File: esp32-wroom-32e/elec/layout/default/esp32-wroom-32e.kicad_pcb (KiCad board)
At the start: 2 copper layers, 225.7 x 100.8 mm, 0 parts

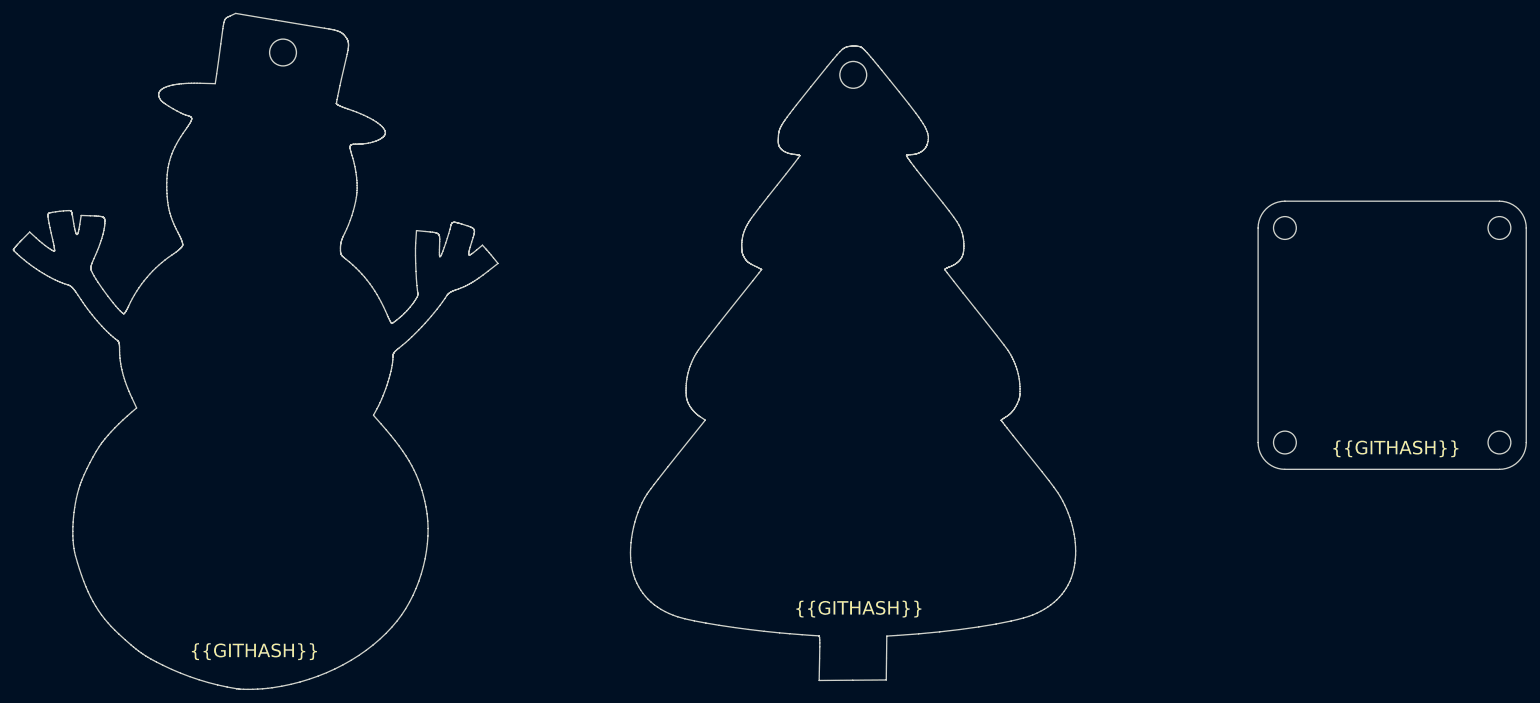
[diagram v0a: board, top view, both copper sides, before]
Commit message: added screw terminals for esp32 pcb
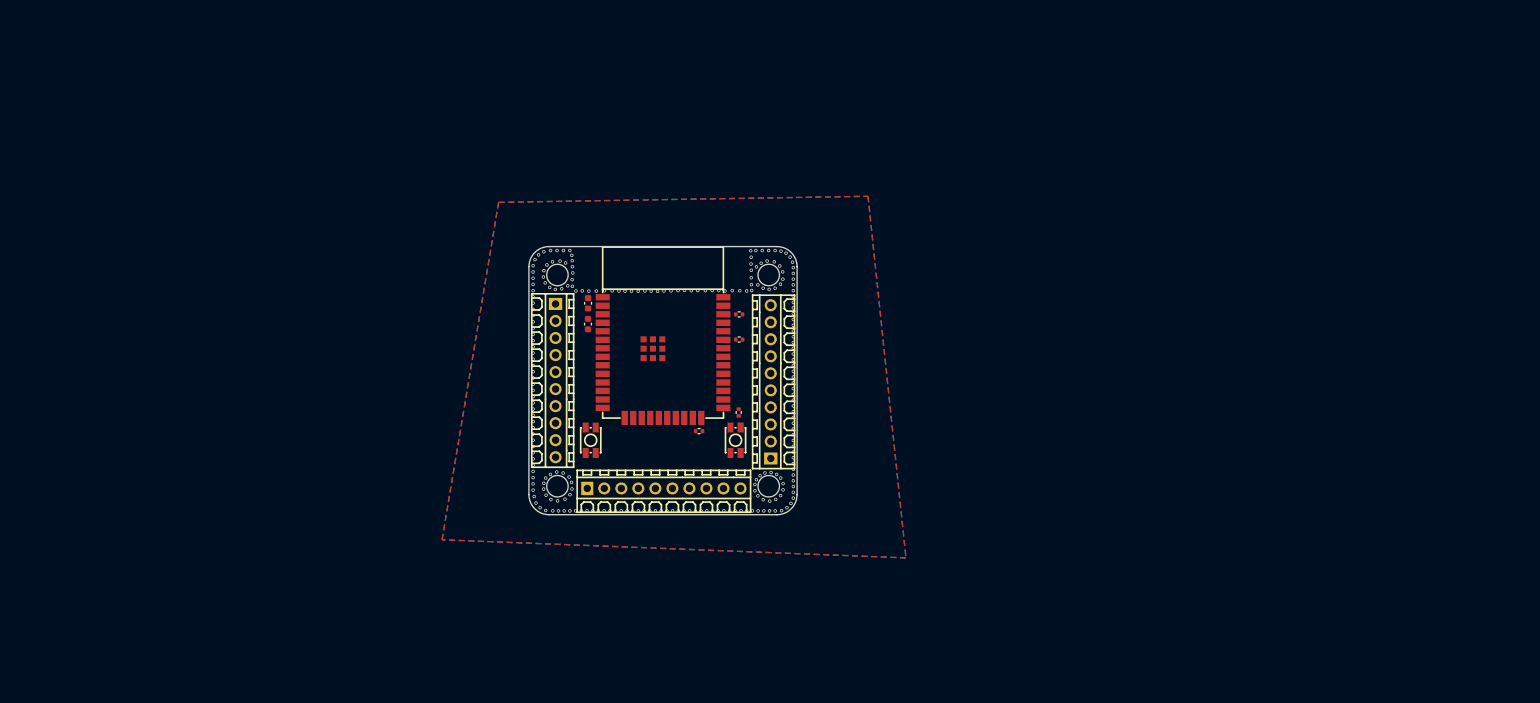
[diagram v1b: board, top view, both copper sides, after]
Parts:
- added C1: 10V 10uF X5R ±10% 0603 Multilayer Ceramic Capacitors MLCC -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, lib:C0603, F.Cu at (121.7, 93.0)
- added C2: 50V 1uF X5R ±10% 0603 Multilayer Ceramic Capacitors MLCC - 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, lib:C0603, F.Cu at (121.7, 96.1)
- added R1: 62.5mW Thick Film Resistors 50V ±100ppm/℃ ±1% 2kΩ 0402 Chip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, lib:R0402, F.Cu at (144.2, 98.4)
- added R2: 62.5mW Thick Film Resistors 50V ±100ppm/℃ ±1% 2kΩ 0402 Chip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, lib:R0402, F.Cu at (144.2, 94.7)
- added R3: 62.5mW Thick Film Resistors 50V ±100ppm/℃ ±1% 5.1kΩ 0402 Ch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, lib:R0402, F.Cu at (138.2, 112.1)
- added R4: 62.5mW Thick Film Resistors 50V ±100ppm/℃ ±1% 100kΩ 0402 Ch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, lib:R0402, F.Cu at (144.1, 109.3)
- added U1: , lib:WIFI-SMD_ESP32-WROOM-32E, F.Cu at (132.8, 101.1)
- added U10: , lib:MountingHole_3.2mm_M3, F.Cu at (117.1, 120.3)
- added U2: , lib:SW-SMD_4P-L3.7-W3.0-P1.50-LS4.7, F.Cu at (143.7, 113.5)
- added U3: , lib:SW-SMD_4P-L3.7-W3.0-P1.50-LS4.7, F.Cu at (122.1, 113.5)
- added U4: , lib:CONN-TH_10P-P2.54_MX128-2.54-10P-GN01-CU-Y-A, F.Cu at (116.8, 104.5)
- added U5: , lib:CONN-TH_10P-P2.54_MX128-2.54-10P-GN01-CU-Y-A, F.Cu at (133.0, 120.6)
- added U6: , lib:CONN-TH_10P-P2.54_MX128-2.54-10P-GN01-CU-Y-A, F.Cu at (148.9, 104.7)
- added U7: , lib:MountingHole_3.2mm_M3, F.Cu at (148.6, 88.8)
- added U8: , lib:MountingHole_3.2mm_M3, F.Cu at (148.6, 120.3)
- added U9: , lib:MountingHole_3.2mm_M3, F.Cu at (117.1, 88.8)
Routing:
- net gnd: vias 0 -> 231
- added copper zone on B.Cu, net gnd
- added copper zone on F.Cu, net gnd
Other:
- board size 225.7 x 100.8 mm -> 40 x 40 mm
- board text removed: "{{GITHASH}}"
